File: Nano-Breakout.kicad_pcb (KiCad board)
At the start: 2 copper layers, 34.3 x 39.4 mm, 3 parts, among them J101 Conn_01x15, J102 Conn_01x15

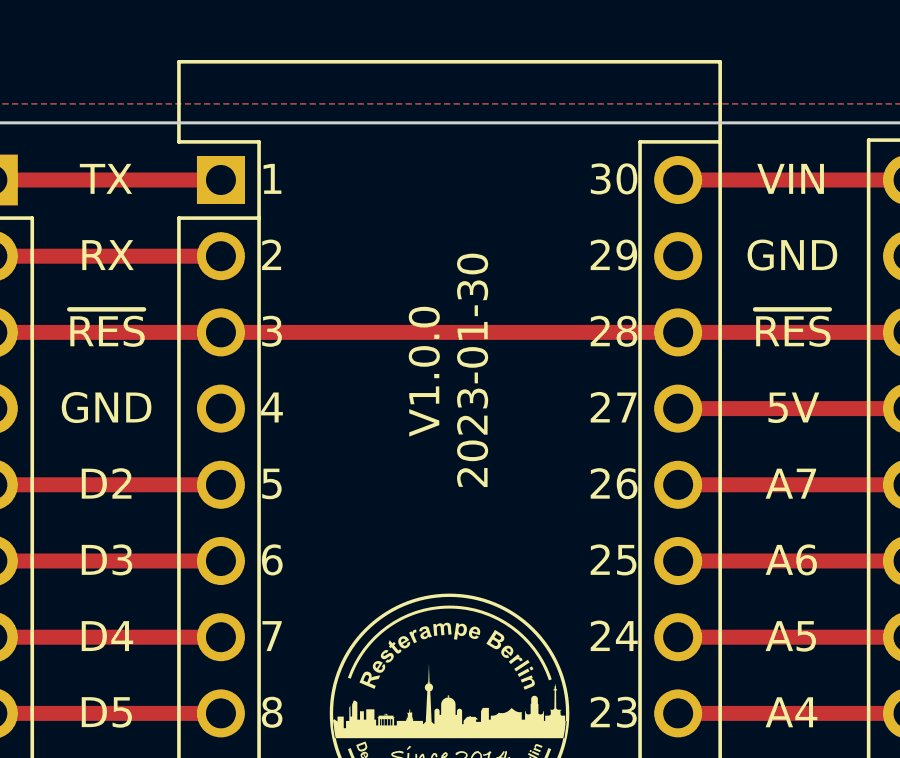
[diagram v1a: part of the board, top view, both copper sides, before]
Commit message: Documentation update, name of board on PCB
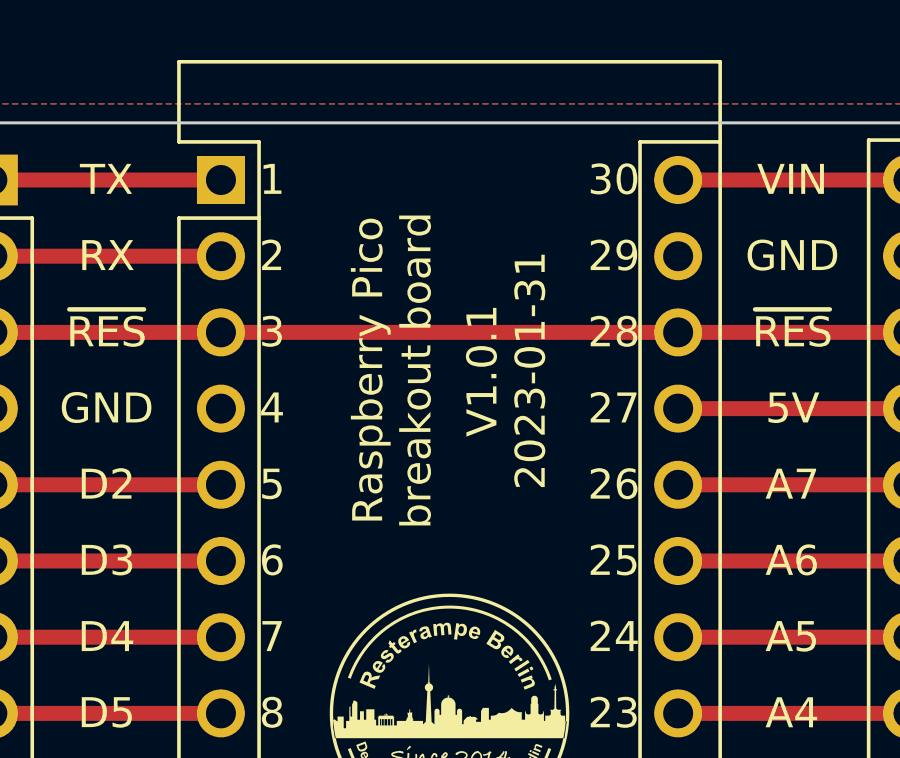
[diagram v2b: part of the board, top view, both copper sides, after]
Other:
- board text added: "Raspberry Pico breakout board"
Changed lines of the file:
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@@
   (title_block
     (title "Arduino Nano breakout board")
-    (date "2023-01-30")
-    (rev "1.0.0")
+    (date "2023-01-31")
+    (rev "1.0.1")
     (company "Resterampe Berlin ")
     (comment 3 "https://creativecommons.org/licenses/by-nc/4.0 ")
@@
     (effects (font (size 1 1) (thickness 0.15)) (justify left))
   )
+  (gr_text "Raspberry Pico\nbreakout board" (at 146.685 78.74 90) (layer "F.SilkS")
+    (effects (font (size 1 1) (thickness 0.15)))
+  )
   (gr_text "5" (at 142.24 82.55) (layer "F.SilkS")
     (effects (font (size 1 1) (thickness 0.15)) (justify left))
@@
     (effects (font (size 1 1) (thickness 0.15)) (justify left))
   )
-  (gr_text "V${REVISION}\n${ISSUE_DATE}\n" (at 148.59 78.74 90) (layer "F.SilkS")
+  (gr_text "V${REVISION}\n${ISSUE_DATE}\n" (at 150.495 78.74 90) (layer "F.SilkS")
     (effects (font (size 1 1) (thickness 0.2)))
   )

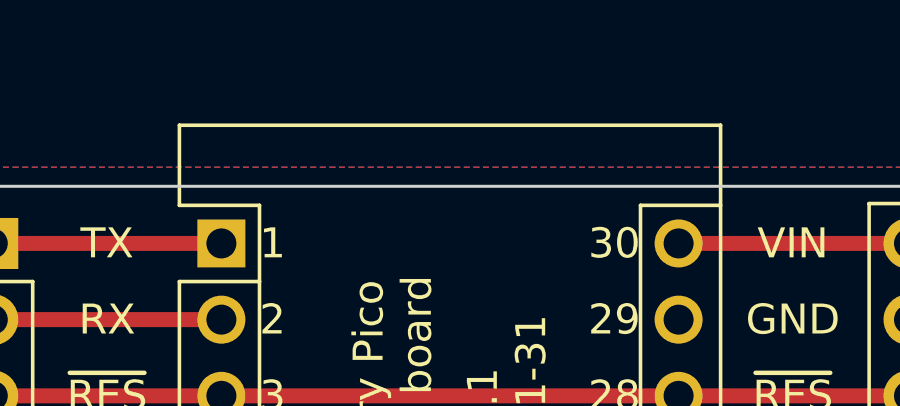
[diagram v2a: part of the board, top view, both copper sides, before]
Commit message: Added 3D stacking header
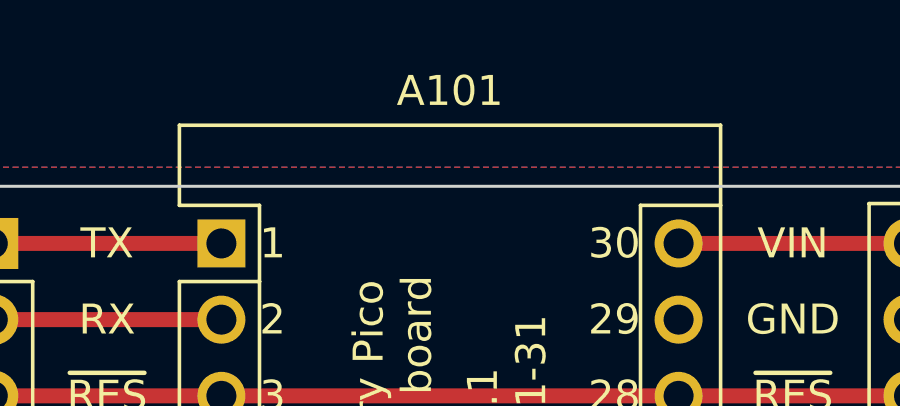
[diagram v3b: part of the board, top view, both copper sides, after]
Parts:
- A101: footprint Module:Arduino_Nano -> Nano:Arduino_Nano
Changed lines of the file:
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@@
       (layer "F.SilkS" (type "Top Silk Screen"))
       (layer "F.Paste" (type "Top Solder Paste"))
-      (layer "F.Mask" (type "Top Solder Mask") (thickness 0.01))
+      (layer "F.Mask" (type "Top Solder Mask") (color "Purple") (thickness 0.01))
       (layer "F.Cu" (type "copper") (thickness 0.035))
       (layer "dielectric 1" (type "core") (thickness 1.51) (material "FR4") (epsilon_r 4.5) (loss_tangent 0.02))
       (layer "B.Cu" (type "copper") (thickness 0.035))
-      (layer "B.Mask" (type "Bottom Solder Mask") (thickness 0.01))
+      (layer "B.Mask" (type "Bottom Solder Mask") (color "Purple") (thickness 0.01))
       (layer "B.Paste" (type "Bottom Solder Paste"))
       (layer "B.SilkS" (type "Bottom Silk Screen"))
@@
     )
   )
-  (footprint "Module:Arduino_Nano" (layer "F.Cu")
+  (footprint "Nano:Arduino_Nano" (layer "F.Cu")
     (at 140.97 72.39)
     (descr "Arduino Nano, http://www.mouser.com/pdfdocs/Gravitech_Arduino_Nano3_0.pdf")
@@
     (property "exclude_from_bom" "")
     (attr through_hole exclude_from_bom)
-    (fp_text reference "A101" (at 7.62 -5.08) (layer "F.SilkS") hide
-      (effects (font (size 1 1) (thickness 0.15)))
-    )
-    (fp_text value "Arduino_Nano_v3.x" (at 8.89 19.05 90) (layer "F.Fab") hide
+    (fp_text reference "A101" (at 7.62 -5.08) (layer "F.SilkS")
+      (effects (font (size 1 1) (thickness 0.15)))
+    )
+    (fp_text value "Arduino_Nano_v3.x" (at 8.89 19.05 90) (layer "F.Fab")
       (effects (font (size 1 1) (thickness 0.15)))
     )
@@
       (effects (font (size 1 1) (thickness 0.15)))
     )
+    (fp_line (start 3.68 31.62) (end 11.56 31.62) (layer "F.SilkS") (width 0.12))
+    (fp_line (start -1.4 1.27) (end -1.4 39.5) (layer "F.SilkS") (width 0.12))
+    (fp_line (start 1.27 1.27) (end 1.27 36.83) (layer "F.SilkS") (width 0.12))
+    (fp_line (start 1.27 -1.27) (end -1.4 -1.27) (layer "F.SilkS") (width 0.12))
+    (fp_line (start 13.97 -1.27) (end 13.97 36.83) (layer "F.SilkS") (width 0.12))
     (fp_line (start 13.97 36.83) (end 16.64 36.83) (layer "F.SilkS") (width 0.12))
+    (fp_line (start 1.27 36.83) (end -1.4 36.83) (layer "F.SilkS") (width 0.12))
+    (fp_line (start 16.64 39.5) (end 11.56 39.5) (layer "F.SilkS") (width 0.12))
     (fp_line (start 11.56 42.04) (end 3.68 42.04) (layer "F.SilkS") (width 0.12))
-    (fp_line (start 16.64 39.5) (end 11.56 39.5) (layer "F.SilkS") (width 0.12))
-    (fp_line (start 3.68 31.62) (end 11.56 31.62) (layer "F.SilkS") (width 0.12))
+    (fp_line (start -1.4 -3.94) (end -1.4 -1.27) (layer "F.SilkS") (width 0.12))
+    (fp_line (start 1.27 1.27) (end -1.4 1.27) (layer "F.SilkS") (width 0.12))
     (fp_line (start -1.4 39.5) (end 3.68 39.5) (layer "F.SilkS") (width 0.12))
-    (fp_line (start 1.27 1.27) (end 1.27 -1.27) (layer "F.SilkS") (width 0.12))
-    (fp_line (start 11.56 31.62) (end 11.56 42.04) (layer "F.SilkS") (width 0.12))
-    (fp_line (start -1.4 1.27) (end -1.4 39.5) (layer "F.SilkS") (width 0.12))
-    (fp_line (start 13.97 -1.27) (end 13.97 36.83) (layer "F.SilkS") (width 0.12))
-    (fp_line (start 1.27 1.27) (end -1.4 1.27) (layer "F.SilkS") (width 0.12))
-    (fp_line (start 1.27 1.27) (end 1.27 36.83) (layer "F.SilkS") (width 0.12))
-    (fp_line (start -1.4 -3.94) (end -1.4 -1.27) (layer "F.SilkS") (width 0.12))
-    (fp_line (start 1.27 36.83) (end -1.4 36.83) (layer "F.SilkS") (width 0.12))
-    (fp_line (start 1.27 -1.27) (end -1.4 -1.27) (layer "F.SilkS") (width 0.12))
-    (fp_line (start 16.64 -3.94) (end -1.4 -3.94) (layer "F.SilkS") (width 0.12))
     (fp_line (start 3.68 42.04) (end 3.68 31.62) (layer "F.SilkS") (width 0.12))
     (fp_line (start 16.64 39.5) (end 16.64 -3.94) (layer "F.SilkS") (width 0.12))
+    (fp_line (start 16.64 -3.94) (end -1.4 -3.94) (layer "F.SilkS") (width 0.12))
+    (fp_line (start 11.56 31.62) (end 11.56 42.04) (layer "F.SilkS") (width 0.12))
     (fp_line (start 13.97 -1.27) (end 16.64 -1.27) (layer "F.SilkS") (width 0.12))
+    (fp_line (start 1.27 1.27) (end 1.27 -1.27) (layer "F.SilkS") (width 0.12))
+    (fp_line (start 16.75 42.16) (end -1.53 42.16) (layer "F.CrtYd") (width 0.05))
+    (fp_line (start -1.53 -4.06) (end -1.53 42.16) (layer "F.CrtYd") (width 0.05))
     (fp_line (start 16.75 42.16) (end 16.75 -4.06) (layer "F.CrtYd") (width 0.05))
     (fp_line (start -1.53 -4.06) (end 16.75 -4.06) (layer "F.CrtYd") (width 0.05))
-    (fp_line (start 16.75 42.16) (end -1.53 42.16) (layer "F.CrtYd") (width 0.05))
-    (fp_line (start -1.53 -4.06) (end -1.53 42.16) (layer "F.CrtYd") (width 0.05))
+    (fp_line (start 11.43 31.75) (end 11.43 41.91) (layer "F.Fab") (width 0.1))
+    (fp_line (start 3.81 31.75) (end 11.43 31.75) (layer "F.Fab") (width 0.1))
     (fp_line (start 16.51 39.37) (end -1.27 39.37) (layer "F.Fab") (width 0.1))
     (fp_line (start 0 -3.81) (end 16.51 -3.81) (layer "F.Fab") (width 0.1))
     (fp_line (start -1.27 39.37) (end -1.27 -2.54) (layer "F.Fab") (width 0.1))
-    (fp_line (start 3.81 31.75) (end 11.43 31.75) (layer "F.Fab") (width 0.1))
-    (fp_line (start 16.51 -3.81) (end 16.51 39.37) (layer "F.Fab") (width 0.1))
-    (fp_line (start 11.43 31.75) (end 11.43 41.91) (layer "F.Fab") (width 0.1))
     (fp_line (start -1.27 -2.54) (end 0 -3.81) (layer "F.Fab") (width 0.1))
     (fp_line (start 11.43 41.91) (end 3.81 41.91) (layer "F.Fab") (width 0.1))
     (fp_line (start 3.81 41.91) (end 3.81 31.75) (layer "F.Fab") (width 0.1))
+    (fp_line (start 16.51 -3.81) (end 16.51 39.37) (layer "F.Fab") (width 0.1))
     (pad "1" thru_hole rect (at 0 0) (size 1.6 1.6) (drill 1) (layers *.Cu *.Mask)
       (net 1 "Net-(A101-Pad1)") (pinfunction "D1/TX") (pintype "bidirectional"))
@@
     (pad "30" thru_hole oval (at 15.24 0) (size 1.6 1.6) (drill 1) (layers *.Cu *.Mask)
       (net 28 "VCC") (pinfunction "VIN") (pintype "power_in"))
-    (model "${KICAD6_3DMODEL_DIR}/Module.3dshapes/Arduino_Nano_WithMountingHoles.wrl"
-      (offset (xyz 0 0 0))
+    (model "${KIPRJMOD}/Stacking header 1x15_15.24mm.step"
+      (offset (xyz 0 -35.57 0))
       (scale (xyz 1 1 1))
-      (rotate (xyz 0 0 0))
+      (rotate (xyz -90 0 -90))
     )
   )

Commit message: Names streamlined
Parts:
- A101: footprint Nano:Arduino_Nano -> Nano:Arduino_Nano_Stacking_THT
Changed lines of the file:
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@@
     )
   )
-  (footprint "Nano:Arduino_Nano" (layer "F.Cu")
+  (footprint "Nano:Arduino_Nano_Stacking_THT" (layer "F.Cu")
     (at 140.97 72.39)
     (descr "Arduino Nano, http://www.mouser.com/pdfdocs/Gravitech_Arduino_Nano3_0.pdf")
@@
       (effects (font (size 1 1) (thickness 0.15)))
     )
+    (fp_line (start 11.56 42.04) (end 3.68 42.04) (layer "F.SilkS") (width 0.12))
+    (fp_line (start 3.68 42.04) (end 3.68 31.62) (layer "F.SilkS") (width 0.12))
+    (fp_line (start -1.4 39.5) (end 3.68 39.5) (layer "F.SilkS") (width 0.12))
     (fp_line (start 3.68 31.62) (end 11.56 31.62) (layer "F.SilkS") (width 0.12))
+    (fp_line (start -1.4 -3.94) (end -1.4 -1.27) (layer "F.SilkS") (width 0.12))
+    (fp_line (start 13.97 -1.27) (end 13.97 36.83) (layer "F.SilkS") (width 0.12))
     (fp_line (start -1.4 1.27) (end -1.4 39.5) (layer "F.SilkS") (width 0.12))
-    (fp_line (start 1.27 1.27) (end 1.27 36.83) (layer "F.SilkS") (width 0.12))
+    (fp_line (start 13.97 36.83) (end 16.64 36.83) (layer "F.SilkS") (width 0.12))
+    (fp_line (start 11.56 31.62) (end 11.56 42.04) (layer "F.SilkS") (width 0.12))
     (fp_line (start 1.27 -1.27) (end -1.4 -1.27) (layer "F.SilkS") (width 0.12))
-    (fp_line (start 13.97 -1.27) (end 13.97 36.83) (layer "F.SilkS") (width 0.12))
-    (fp_line (start 13.97 36.83) (end 16.64 36.83) (layer "F.SilkS") (width 0.12))
+    (fp_line (start 16.64 39.5) (end 11.56 39.5) (layer "F.SilkS") (width 0.12))
     (fp_line (start 1.27 36.83) (end -1.4 36.83) (layer "F.SilkS") (width 0.12))
-    (fp_line (start 16.64 39.5) (end 11.56 39.5) (layer "F.SilkS") (width 0.12))
-    (fp_line (start 11.56 42.04) (end 3.68 42.04) (layer "F.SilkS") (width 0.12))
-    (fp_line (start -1.4 -3.94) (end -1.4 -1.27) (layer "F.SilkS") (width 0.12))
+    (fp_line (start 16.64 -3.94) (end -1.4 -3.94) (layer "F.SilkS") (width 0.12))
     (fp_line (start 1.27 1.27) (end -1.4 1.27) (layer "F.SilkS") (width 0.12))
-    (fp_line (start -1.4 39.5) (end 3.68 39.5) (layer "F.SilkS") (width 0.12))
-    (fp_line (start 3.68 42.04) (end 3.68 31.62) (layer "F.SilkS") (width 0.12))
     (fp_line (start 16.64 39.5) (end 16.64 -3.94) (layer "F.SilkS") (width 0.12))
-    (fp_line (start 16.64 -3.94) (end -1.4 -3.94) (layer "F.SilkS") (width 0.12))
-    (fp_line (start 11.56 31.62) (end 11.56 42.04) (layer "F.SilkS") (width 0.12))
     (fp_line (start 13.97 -1.27) (end 16.64 -1.27) (layer "F.SilkS") (width 0.12))
     (fp_line (start 1.27 1.27) (end 1.27 -1.27) (layer "F.SilkS") (width 0.12))
+    (fp_line (start 1.27 1.27) (end 1.27 36.83) (layer "F.SilkS") (width 0.12))
+    (fp_line (start 16.75 42.16) (end 16.75 -4.06) (layer "F.CrtYd") (width 0.05))
     (fp_line (start 16.75 42.16) (end -1.53 42.16) (layer "F.CrtYd") (width 0.05))
     (fp_line (start -1.53 -4.06) (end -1.53 42.16) (layer "F.CrtYd") (width 0.05))
-    (fp_line (start 16.75 42.16) (end 16.75 -4.06) (layer "F.CrtYd") (width 0.05))
     (fp_line (start -1.53 -4.06) (end 16.75 -4.06) (layer "F.CrtYd") (width 0.05))
+    (fp_line (start 0 -3.81) (end 16.51 -3.81) (layer "F.Fab") (width 0.1))
+    (fp_line (start 3.81 41.91) (end 3.81 31.75) (layer "F.Fab") (width 0.1))
+    (fp_line (start 3.81 31.75) (end 11.43 31.75) (layer "F.Fab") (width 0.1))
+    (fp_line (start -1.27 -2.54) (end 0 -3.81) (layer "F.Fab") (width 0.1))
+    (fp_line (start 16.51 39.37) (end -1.27 39.37) (layer "F.Fab") (width 0.1))
     (fp_line (start 11.43 31.75) (end 11.43 41.91) (layer "F.Fab") (width 0.1))
-    (fp_line (start 3.81 31.75) (end 11.43 31.75) (layer "F.Fab") (width 0.1))
-    (fp_line (start 16.51 39.37) (end -1.27 39.37) (layer "F.Fab") (width 0.1))
-    (fp_line (start 0 -3.81) (end 16.51 -3.81) (layer "F.Fab") (width 0.1))
+    (fp_line (start 16.51 -3.81) (end 16.51 39.37) (layer "F.Fab") (width 0.1))
+    (fp_line (start 11.43 41.91) (end 3.81 41.91) (layer "F.Fab") (width 0.1))
     (fp_line (start -1.27 39.37) (end -1.27 -2.54) (layer "F.Fab") (width 0.1))
-    (fp_line (start -1.27 -2.54) (end 0 -3.81) (layer "F.Fab") (width 0.1))
-    (fp_line (start 11.43 41.91) (end 3.81 41.91) (layer "F.Fab") (width 0.1))
-    (fp_line (start 3.81 41.91) (end 3.81 31.75) (layer "F.Fab") (width 0.1))
-    (fp_line (start 16.51 -3.81) (end 16.51 39.37) (layer "F.Fab") (width 0.1))
     (pad "1" thru_hole rect (at 0 0) (size 1.6 1.6) (drill 1) (layers *.Cu *.Mask)
       (net 1 "Net-(A101-Pad1)") (pinfunction "D1/TX") (pintype "bidirectional"))
@@
     (pad "30" thru_hole oval (at 15.24 0) (size 1.6 1.6) (drill 1) (layers *.Cu *.Mask)
       (net 28 "VCC") (pinfunction "VIN") (pintype "power_in"))
-    (model "${KIPRJMOD}/Stacking header 1x15_15.24mm.step"
-      (offset (xyz 0 -35.57 0))
+    (model "${KIPRJMOD}/Stacking header 2x15_15.24mm.step"
+      (offset (xyz 15.24 0 0))
       (scale (xyz 1 1 1))
-      (rotate (xyz -90 0 -90))
+      (rotate (xyz -90 0 90))
     )
   )
